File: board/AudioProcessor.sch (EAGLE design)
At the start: 46 parts, among them IC1 LP2951, IC2 ATTINY24/44/84-SSU, IC3 TDA7439DS, IC4 LP2951, J1 PINHD-1X3-JST-PH, J2 PINHD-1X3-JST-PH, J3 PINHD-1X3-JST-PH, J4 PINHD-1X3-JST-PH, J5 PINHD-1X6-JST-PH, J6 PINHD-1X3-JST-PH

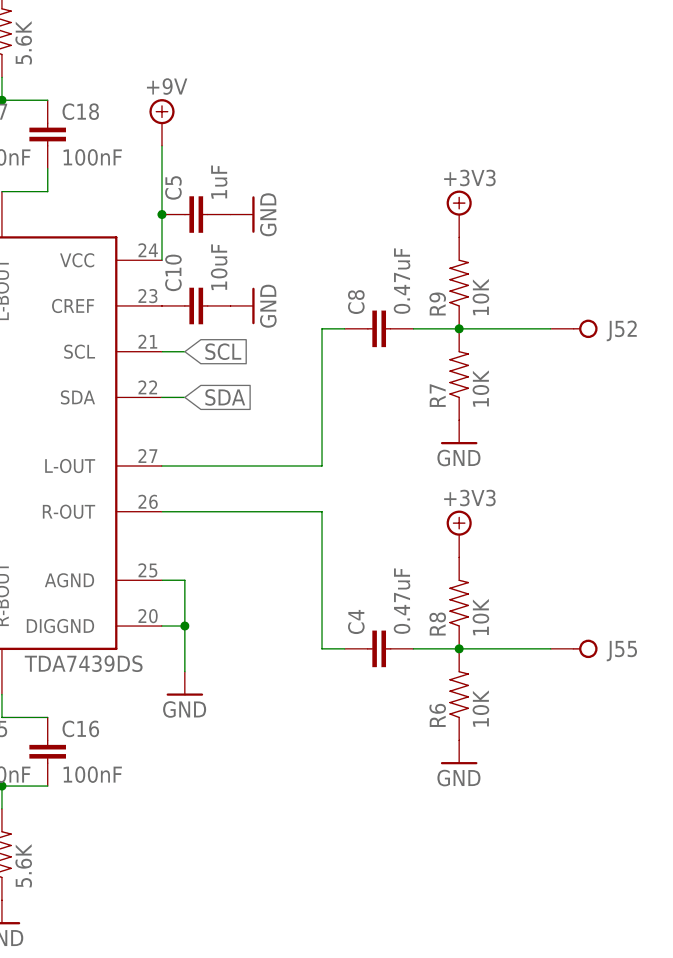
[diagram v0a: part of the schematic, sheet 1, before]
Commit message: Removed unnecessary output biasing
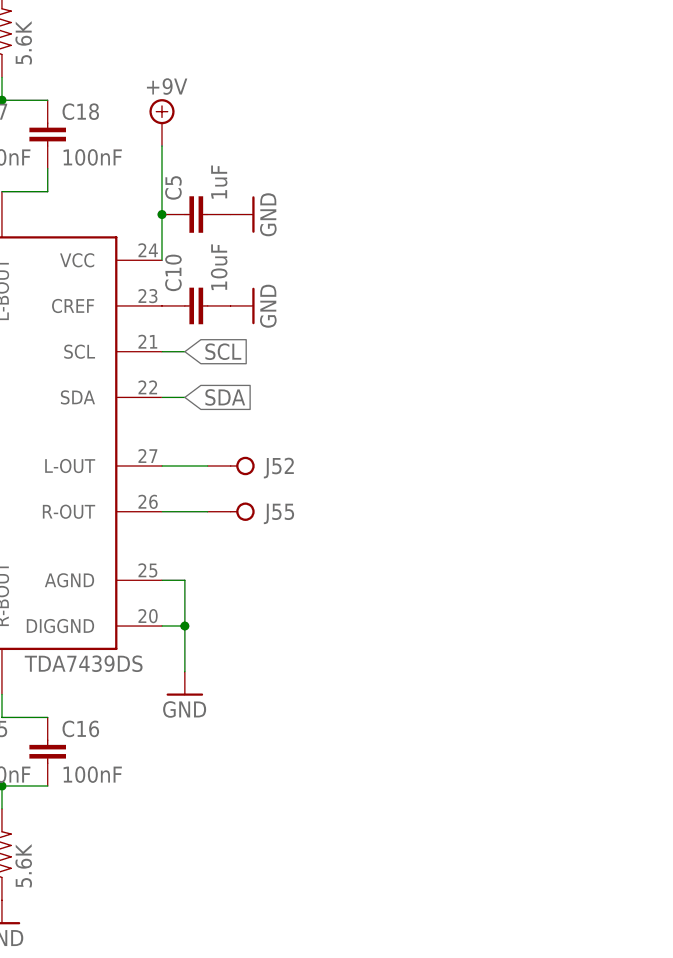
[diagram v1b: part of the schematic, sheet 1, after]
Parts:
- removed C4, C8: 0.47uF, SaintGimp:CAPACITOR-5MM
- removed R6, R7, R8, R9: 10K, SaintGimp:RESISTOR-0805
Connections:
- removed net L-OUT-BIASED: C8.2, J52.KL, R7.2, R9.1
- removed net R-OUT-BIASED: C4.2, J55.KL, R6.2, R8.1
- net +3V3: no longer R8.2, R9.2
- net GND: no longer R6.1, R7.1
- net L-OUT: now also J52.KL; no longer C8.1
- net R-OUT: now also J55.KL; no longer C4.1
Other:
- moved on the sheet: J52, J55
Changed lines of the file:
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@@
 <part name="GND19" library="SaintGimp" deviceset="GND" device=""/>
 <part name="GND26" library="SaintGimp" deviceset="GND" device=""/>
-<part name="R9" library="SaintGimp" deviceset="RESISTOR-*" device="0805" value="10K"/>
-<part name="R7" library="SaintGimp" deviceset="RESISTOR-*" device="0805" value="10K"/>
-<part name="GND12" library="SaintGimp" deviceset="GND" device=""/>
-<part name="C8" library="SaintGimp" deviceset="CAPACITOR-*" device="5MM" value="0.47uF"/>
-<part name="R8" library="SaintGimp" deviceset="RESISTOR-*" device="0805" value="10K"/>
-<part name="R6" library="SaintGimp" deviceset="RESISTOR-*" device="0805" value="10K"/>
-<part name="GND13" library="SaintGimp" deviceset="GND" device=""/>
-<part name="C4" library="SaintGimp" deviceset="CAPACITOR-*" device="5MM" value="0.47uF"/>
 <part name="P+9" library="SaintGimp" deviceset="VCC" device=""/>
 <part name="C6" library="SaintGimp" deviceset="CAPACITOR-*" device="1206" value="10uF"/>
@@
 <part name="P+15" library="SaintGimp" deviceset="+3V3" device=""/>
 <part name="P+11" library="SaintGimp" deviceset="+3V3" device=""/>
-<part name="P+2" library="SaintGimp" deviceset="+3V3" device=""/>
-<part name="P+3" library="SaintGimp" deviceset="+3V3" device=""/>
 <part name="P+13" library="SaintGimp" deviceset="+3V3" device=""/>
 <part name="GND24" library="SaintGimp" deviceset="GND" device=""/>
@@
 <instance part="C10" gate="G$1" x="114.3" y="58.42" rot="R90"/>
 <instance part="GND11" gate="1" x="119.38" y="58.42" rot="R90"/>
-<instance part="R9" gate="G$1" x="142.24" y="60.96" rot="R90"/>
-<instance part="R7" gate="G$1" x="142.24" y="50.8" rot="R90"/>
-<instance part="GND12" gate="1" x="142.24" y="43.18"/>
-<instance part="C8" gate="G$1" x="134.62" y="55.88" rot="R90"/>
-<instance part="R8" gate="G$1" x="142.24" y="25.4" rot="R90"/>
-<instance part="R6" gate="G$1" x="142.24" y="15.24" rot="R90"/>
-<instance part="GND13" gate="1" x="142.24" y="7.62"/>
-<instance part="C4" gate="G$1" x="134.62" y="20.32" rot="R90"/>
 <instance part="C5" gate="G$1" x="114.3" y="68.58" rot="R90"/>
 <instance part="GND10" gate="1" x="119.38" y="68.58" rot="R90"/>
-<instance part="P+2" gate="G$1" x="142.24" y="68.58"/>
-<instance part="P+3" gate="G$1" x="142.24" y="33.02"/>
 <instance part="P+1" gate="G$1" x="109.22" y="78.74"/>
 <instance part="C9" gate="G$1" x="33.02" y="55.88" rot="R90"/>
 <instance part="C3" gate="G$1" x="33.02" y="35.56" rot="R90"/>
 <instance part="J5" gate="1" x="20.32" y="55.88"/>
-<instance part="J5" gate="2" x="157.48" y="55.88" rot="R180"/>
+<instance part="J5" gate="2" x="119.38" y="40.64" rot="R180"/>
 <instance part="J5" gate="3" x="22.86" y="10.16"/>
 <instance part="J5" gate="4" x="22.86" y="5.08"/>
-<instance part="J5" gate="5" x="157.48" y="20.32" rot="R180"/>
+<instance part="J5" gate="5" x="119.38" y="35.56" rot="R180"/>
 <instance part="J5" gate="6" x="20.32" y="35.56"/>
 <instance part="GND2" gate="1" x="30.48" y="5.08" rot="R90"/>
@@
 </segment>
 <segment>
-<pinref part="R7" gate="G$1" pin="1"/>
-<pinref part="GND12" gate="1" pin="GND"/>
-</segment>
-<segment>
-<pinref part="R6" gate="G$1" pin="1"/>
-<pinref part="GND13" gate="1" pin="GND"/>
-</segment>
-<segment>
 <pinref part="C5" gate="G$1" pin="2"/>
 <pinref part="GND10" gate="1" pin="GND"/>
@@
 </segment>
 </net>
-<net name="L-OUT-BIASED" class="0">
-<segment>
-<pinref part="R9" gate="G$1" pin="1"/>
-<pinref part="R7" gate="G$1" pin="2"/>
-<junction x="142.24" y="55.88"/>
-<wire x1="142.24" y1="55.88" x2="152.4" y2="55.88" width="0.1524" layer="91"/>
-<pinref part="C8" gate="G$1" pin="2"/>
-<wire x1="137.16" y1="55.88" x2="142.24" y2="55.88" width="0.1524" layer="91"/>
+<net name="L-OUT" class="0">
+<segment>
+<pinref part="IC3" gate="G$1" pin="L-OUT"/>
+<wire x1="114.3" y1="40.64" x2="109.22" y2="40.64" width="0.1524" layer="91"/>
 <pinref part="J5" gate="2" pin="KL"/>
 </segment>
 </net>
-<net name="L-OUT" class="0">
-<segment>
-<pinref part="C8" gate="G$1" pin="1"/>
-<wire x1="129.54" y1="55.88" x2="127" y2="55.88" width="0.1524" layer="91"/>
-<wire x1="127" y1="55.88" x2="127" y2="40.64" width="0.1524" layer="91"/>
-<pinref part="IC3" gate="G$1" pin="L-OUT"/>
-<wire x1="127" y1="40.64" x2="109.22" y2="40.64" width="0.1524" layer="91"/>
-</segment>
-</net>
-<net name="R-OUT-BIASED" class="0">
-<segment>
-<pinref part="R8" gate="G$1" pin="1"/>
-<pinref part="R6" gate="G$1" pin="2"/>
-<junction x="142.24" y="20.32"/>
-<wire x1="142.24" y1="20.32" x2="152.4" y2="20.32" width="0.1524" layer="91"/>
-<pinref part="C4" gate="G$1" pin="2"/>
-<wire x1="137.16" y1="20.32" x2="142.24" y2="20.32" width="0.1524" layer="91"/>
+<net name="R-OUT" class="0">
+<segment>
+<pinref part="IC3" gate="G$1" pin="R-OUT"/>
+<wire x1="109.22" y1="35.56" x2="114.3" y2="35.56" width="0.1524" layer="91"/>
 <pinref part="J5" gate="5" pin="KL"/>
 </segment>
 </net>
-<net name="R-OUT" class="0">
-<segment>
-<pinref part="C4" gate="G$1" pin="1"/>
-<wire x1="129.54" y1="20.32" x2="127" y2="20.32" width="0.1524" layer="91"/>
-<pinref part="IC3" gate="G$1" pin="R-OUT"/>
-<wire x1="109.22" y1="35.56" x2="127" y2="35.56" width="0.1524" layer="91"/>
-<wire x1="127" y1="35.56" x2="127" y2="20.32" width="0.1524" layer="91"/>
-</segment>
-</net>
-<net name="+3V3" class="0">
-<segment>
-<pinref part="R9" gate="G$1" pin="2"/>
-<pinref part="P+2" gate="G$1" pin="+3V3"/>
-</segment>
-<segment>
-<pinref part="R8" gate="G$1" pin="2"/>
-<pinref part="P+3" gate="G$1" pin="+3V3"/>
-</segment>
-</net>

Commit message: Add status LED and other improvements
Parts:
- removed C19: 22nF, SaintGimp:CAPACITOR-5MM
- removed C20: 18nF, SaintGimp:CAPACITOR-5MM
- removed R13, R14: 2.7K, SaintGimp:RESISTOR-0805
- removed R15: 5.6K, SaintGimp:RESISTOR-0805
- added C4: 0.47uF, SaintGimp:CAPACITOR-5MM
- added C8: 5.6nF, SaintGimp:CAPACITOR-5MM
- added D1: LED-0805, SaintGimp:LED-0805
- added D2: DIODE-DO214AC, SaintGimp:DIODE-DO214AC
- added R6: 470, SaintGimp:RESISTOR-0805
- added R7: 620K, SaintGimp:RESISTOR-0805
- added R8: 100K, SaintGimp:RESISTOR-0805
- added R9: 5.6K, SaintGimp:RESISTOR-0805
- C1: value 10uF -> 0.1uF; device SaintGimp:CAPACITOR-1206 -> SaintGimp:CAPACITOR-0805
- C10: value 10uF -> 5.6nF; device SaintGimp:CAPACITOR-1206 -> SaintGimp:CAPACITOR-5MM
- C11: value 5.6nF -> 18nF
- C12: value 5.6nF -> 22nF
- C13: value 18nF -> 100nF
- C14: value 22nF -> 100nF
- C17: value 100nF -> 22nF
- C18: value 100nF -> 18nF
- C2: value 1uF -> 10uF; device SaintGimp:CAPACITOR-0805 -> SaintGimp:CAPACITOR-1206
- C3: value 0.47uF -> 10uF; device SaintGimp:CAPACITOR-5MM -> SaintGimp:CAPACITOR-1206
- C5: value 1uF -> 0.1uF
- C7: value 470uF -> 0.47uF; device SaintGimp:CAP-POL-5-8 -> SaintGimp:CAPACITOR-5MM
- C9: value 0.47uF -> 470uF; device SaintGimp:CAPACITOR-5MM -> SaintGimp:CAP-POL-
- IC1: value LP2951 -> ATTINY24/44/84-SSU; device SaintGimp:LP2951 -> SaintGimp:ATTINY24/44/84-SSU
- IC2: value ATTINY24/44/84-SSU -> LP2951; device SaintGimp:ATTINY24/44/84-SSU -> SaintGimp:LP2951
- IC3: value TDA7439DS -> LP2951; device SaintGimp:TDA7439DS -> SaintGimp:LP2951
- IC4: value LP2951 -> TDA7439DS; device SaintGimp:LP2951 -> SaintGimp:TDA7439DS
- J5: value PINHD-1X6-JST-PH -> PINHD-1X3-JST-PH; device SaintGimp:PINHD-1X6-JST-PH -> SaintGimp:PINHD-1X3-JST-PH
- J6: value PINHD-1X3-JST-PH -> PINHD-1X6-JST-PH; device SaintGimp:PINHD-1X3-JST-PH -> SaintGimp:PINHD-1X6-JST-PH
- R1: value 10K -> 470
- R10: value 620K -> 2.7K
- R11: value 100K -> 2.7K
- R4: value 470 -> 10K
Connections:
- new net LED: IC1.PB3, R6.2
- new net N$18: C9.+, D2.-, IC3.VIN
- new net N$2: D1.A, R6.1
- net +3V3: now also C1.2, C2.1, IC1.VCC, IC2.OUT, IC2.SENSE, R4.1; no longer C1.1, C2.2, IC1.OUT, IC1.SENSE, IC2.VCC, R1.1
- net +9V: now also C3.1, IC2.VIN, IC3.OUT, IC4.VCC, R7.2; no longer C6.1, IC1.VIN, IC3.VCC, IC4.OUT, R10.2
- net BASS: now also IC1.PA3, J43.KL; no longer IC2.PA3, J42.KL
- net GND: now also C1.1, C10.1, C2.2, C3.2, C8.1, C9.-, D1.C, IC2.SHDWN, IC3.GND, IC4.AGND, IC4.DIGGND, J12.KL, J22.KL, J32.KL, J42.KL, J52.KL, J63.KL, J64.KL, R10.2, R12.2, R8.1, R9.1; no longer C1.2, C10.2, C11.1, C12.1, C2.1, C7.-, IC1.SHDWN, IC3.AGND, IC3.DIGGND, IC4.GND, J13.KL, J23.KL, J33.KL, J43.KL, J53.KL, J54.KL, J62.KL, R12.1, R13.1, R14.2, R15.2
- net L-IN: now also C7.2, IC4.L-IN2; no longer C9.2, IC3.L-IN2
- net L-IN-RAW: now also C7.1, J66.KL; no longer C9.1, J51.KL
- net L-OUT: now also IC4.L-OUT, J65.KL; no longer IC3.L-OUT, J52.KL
- net MID: now also IC1.PA2, J33.KL; no longer IC2.PA2, J32.KL
- net MISO: now also IC1.PA5; no longer IC2.PA5
- net MOSI: now also IC1.PA6, R2.1; no longer IC2.PA6, R4.1
- net N$1: now also C10.2, IC4.L-TREBLE; no longer C12.2, IC3.L-TREBLE
- net N$10: now also C11.1, IC4.R-MIN; no longer C13.1, IC3.R-MIN
- net N$11: now also C12.1, IC4.R-MOUT; no longer C14.1, IC3.R-MOUT
- net N$12: now also C11.2, C12.2, R11.2; no longer C13.2, C14.2, R13.2
- net N$13: now also C13.2, C14.2, R9.2; no longer C15.2, C16.2, R12.2
- net N$14: now also C14.1, IC4.R-BOUT; no longer C16.1, IC3.R-BOUT
- net N$15: now also C13.1, IC4.R-BIN; no longer C15.1, IC3.R-BIN
- net N$16: now also C6.1, IC4.CREF; no longer C10.1, IC3.CREF
- net N$17: now also IC3.FB, R7.1, R8.2; no longer IC4.FB, R10.1, R11.2
- net N$19: now also IC2.FB, IC2.VTAP; no longer IC1.FB, IC1.VTAP
- net N$3: now also C18.2, IC4.L-MIN; no longer C20.2, IC3.L-MIN
- net N$4: now also C17.2, IC4.L-MOUT; no longer C19.2, IC3.L-MOUT
- net N$5: now also C17.1, C18.1, R10.1; no longer C19.1, C20.1, R14.1
- net N$6: now also C15.2, IC4.L-BIN; no longer C17.2, IC3.L-BIN
- net N$7: now also C16.2, IC4.L-BOUT; no longer C18.2, IC3.L-BOUT
- net N$8: now also C15.1, C16.1, R12.1; no longer C17.1, C18.1, R15.1
- net N$9: now also C8.2, IC4.R-TREBLE; no longer C11.2, IC3.R-TREBLE
- net R-IN: now also C4.2, IC4.R-IN2; no longer C3.2, IC3.R-IN2
- net R-IN-RAW: now also C4.1, J61.KL; no longer C3.1, J56.KL
- net R-OUT: now also IC4.R-OUT, J62.KL; no longer IC3.R-OUT, J55.KL
- net RST: now also IC1.PB2, R3.2; no longer IC2.PB2, R1.2
- net SCK: now also IC1.PA4, R1.1; no longer IC2.PA4, R2.1
- net SCL: now also IC4.SCL, R1.2, R4.2; no longer IC3.SCL, R2.2, R3.2
- net SDA: now also IC4.SDA, R2.2; no longer IC3.SDA, R4.2
- net SHUTDOWN: now also IC3.SHDWN, J53.KL; no longer IC4.SHDWN, J63.KL
- net TREBLE: now also IC1.PA1, J23.KL; no longer IC2.PA1, J22.KL
- net VCC: now also D2.+, J51.KL; no longer C7.+, IC4.VIN, J61.KL
- net VOLUME: now also IC1.PA0, J13.KL; no longer IC2.PA0, J12.KL

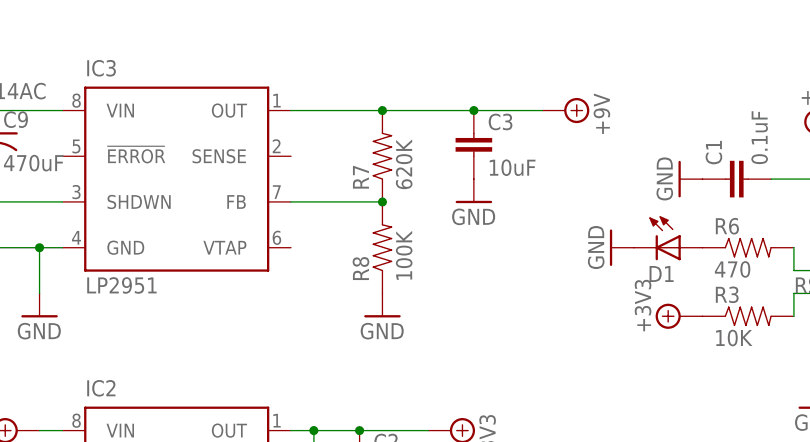
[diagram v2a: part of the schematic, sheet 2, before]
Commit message: Change regulator programming resistor to a value that matches house part availability and still gives us an acceptable output voltage.
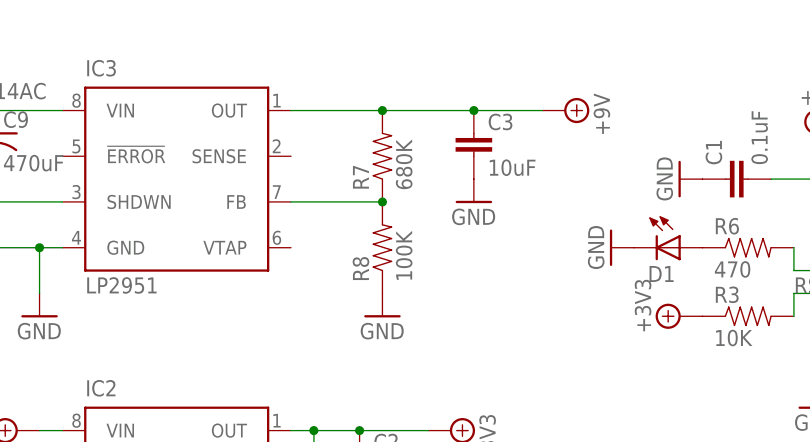
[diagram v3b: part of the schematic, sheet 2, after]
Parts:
- R7: value 620K -> 680K
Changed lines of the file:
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@@
 <?xml version="1.0" encoding="utf-8"?>
 <!DOCTYPE eagle SYSTEM "eagle.dtd">
-<eagle version="8.0.0">
+<eagle version="8.3.2">
 <drawing>
 <settings>
 <setting alwaysvectorfont="no"/>
+<setting keepoldvectorfont="yes"/>
 <setting verticaltext="up"/>
 </settings>
@@
 <part name="IC2" library="SaintGimp" deviceset="LP2951" device=""/>
 <part name="GND20" library="SaintGimp" deviceset="GND" device=""/>
-<part name="R7" library="SaintGimp" deviceset="RESISTOR-*" device="0805" value="620K"/>
+<part name="R7" library="SaintGimp" deviceset="RESISTOR-*" device="0805" value="680K"/>
 <part name="R8" library="SaintGimp" deviceset="RESISTOR-*" device="0805" value="100K"/>
 <part name="GND22" library="SaintGimp" deviceset="GND" device=""/>
